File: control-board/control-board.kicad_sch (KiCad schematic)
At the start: 65 parts, among them J1 LED ch 1-16, J10 ESP32 left (3V3 row), J11 ESP32 right (GND row), J12 24V IN, J2 LED ch 17-32, J3 LED ch 33-48, J4 LED ch 49-64, J5 LED ch 65-80, J6 LED ch 81-96, J7 24V IN (5.5/2.5), J8 FAN 24V, J9 logic/analog, Q1 AO3400A, SW1 MODE, SW2 UP, SW3 DOWN, U101 PCA9685PW (0x40), U102 PCA9685PW (0x41), U103 PCA9685PW (0x42), U104 PCA9685PW (0x43), U105 PCA9685PW (0x44), U106 PCA9685PW (0x45), U110 XL1509-5.0E1, U111 ADS1115IDGS (DNP)

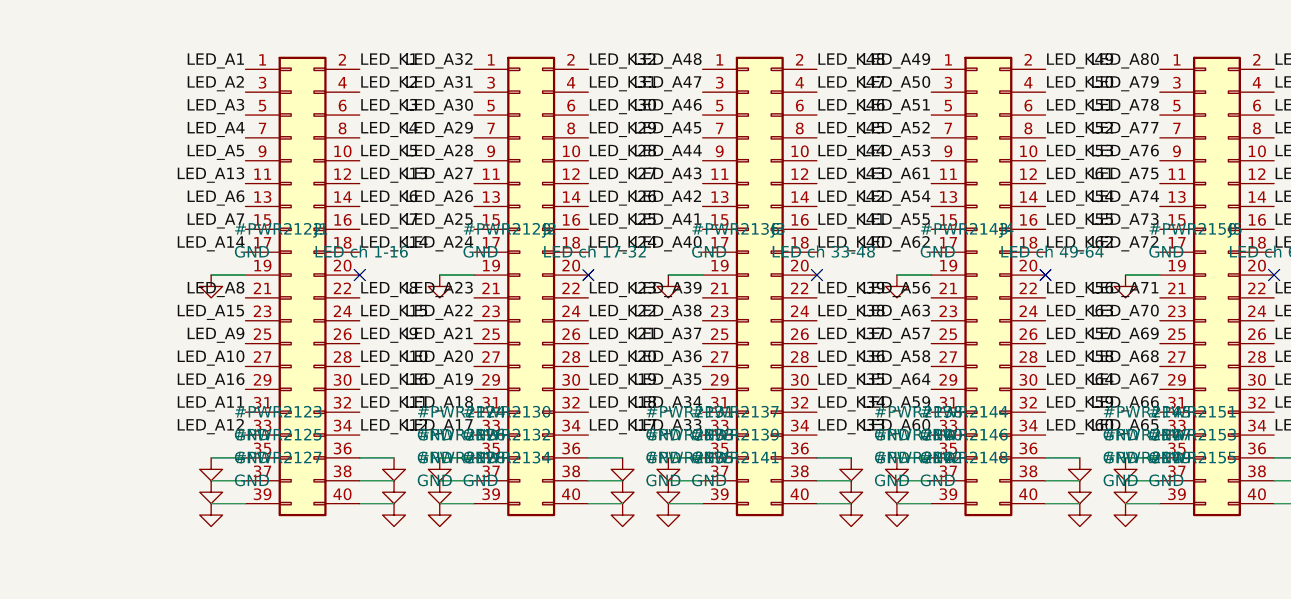
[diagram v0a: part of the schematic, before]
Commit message: LED board support parts copied to control-board topology (15mm border kept)
J1/J4 vertical on left edge, J2/J3 top, J5/J6 bottom, mux stack +
J9 on right strip; pin_maps v6 (CONN_MAP re-optimized, NTC_MAP
re-derived for right-strip muxes); schematics regenerated, netlists
verified, pads re-netted, zones refilled. New scripts:
layout_led_support.py, apply_netlist.py.

Co-Authored-By: Claude Fable 5 <noreply@anthropic.com>
Claude-Session: https://claude.ai/code/session_017oD54uh7Tvu54u9NPQNcZB
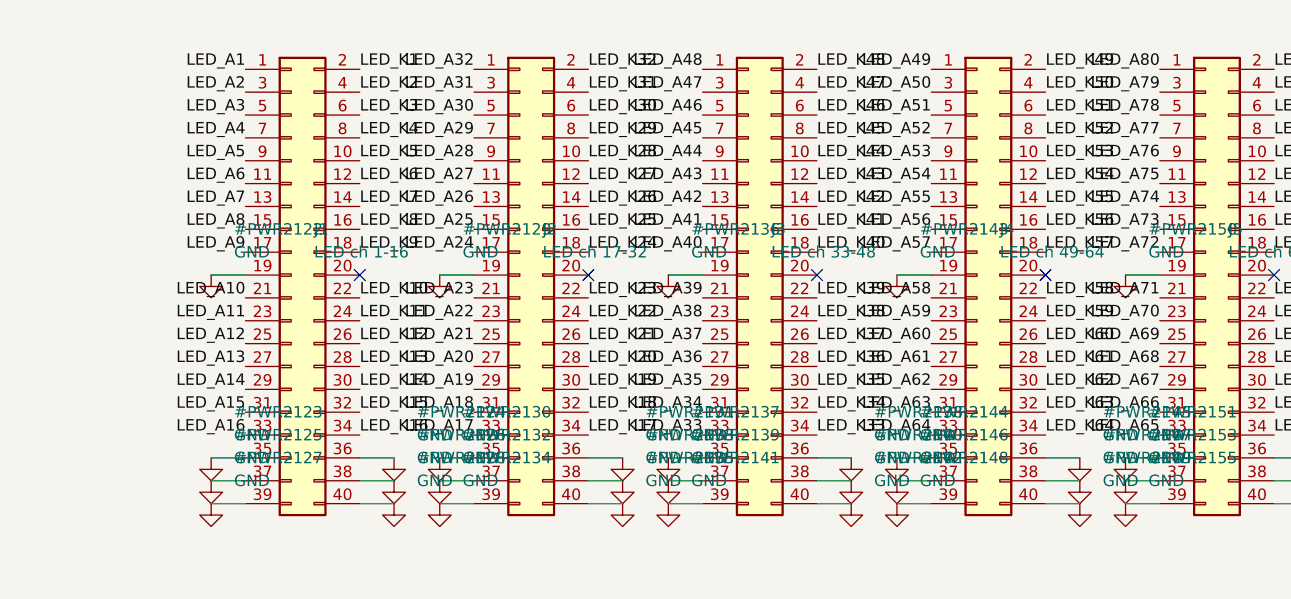
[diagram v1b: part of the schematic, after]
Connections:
- net LED_A10: now also J1.21 (Pin_21); no longer J1.27 (Pin_27)
- net LED_A11: now also J1.23 (Pin_23); no longer J1.31 (Pin_31)
- net LED_A12: now also J1.25 (Pin_25); no longer J1.33 (Pin_33)
- net LED_A13: now also J1.27 (Pin_27); no longer J1.11 (Pin_11)
- net LED_A14: now also J1.29 (Pin_29); no longer J1.17 (Pin_17)
- net LED_A15: now also J1.31 (Pin_31); no longer J1.23 (Pin_23)
- net LED_A16: now also J1.33 (Pin_33); no longer J1.29 (Pin_29)
- net LED_A54: now also J4.11 (Pin_11); no longer J4.13 (Pin_13)
- net LED_A55: now also J4.13 (Pin_13); no longer J4.15 (Pin_15)
- net LED_A56: now also J4.15 (Pin_15); no longer J4.21 (Pin_21)
- net LED_A57: now also J4.17 (Pin_17); no longer J4.25 (Pin_25)
- net LED_A58: now also J4.21 (Pin_21); no longer J4.27 (Pin_27)
- net LED_A59: now also J4.23 (Pin_23); no longer J4.31 (Pin_31)
- net LED_A6: now also J1.11 (Pin_11); no longer J1.13 (Pin_13)
- net LED_A60: now also J4.25 (Pin_25); no longer J4.33 (Pin_33)
- net LED_A61: now also J4.27 (Pin_27); no longer J4.11 (Pin_11)
- net LED_A62: now also J4.29 (Pin_29); no longer J4.17 (Pin_17)
- net LED_A63: now also J4.31 (Pin_31); no longer J4.23 (Pin_23)
- net LED_A64: now also J4.33 (Pin_33); no longer J4.29 (Pin_29)
- net LED_A7: now also J1.13 (Pin_13); no longer J1.15 (Pin_15)
- net LED_A8: now also J1.15 (Pin_15); no longer J1.21 (Pin_21)
- net LED_A9: now also J1.17 (Pin_17); no longer J1.25 (Pin_25)
- net LED_K10: now also J1.22 (Pin_22); no longer J1.28 (Pin_28)
- net LED_K11: now also J1.24 (Pin_24); no longer J1.32 (Pin_32)
- net LED_K12: now also J1.26 (Pin_26); no longer J1.34 (Pin_34)
- net LED_K13: now also J1.28 (Pin_28); no longer J1.12 (Pin_12)
- net LED_K14: now also J1.30 (Pin_30); no longer J1.18 (Pin_18)
- net LED_K15: now also J1.32 (Pin_32); no longer J1.24 (Pin_24)
- net LED_K16: now also J1.34 (Pin_34); no longer J1.30 (Pin_30)
- net LED_K54: now also J4.12 (Pin_12); no longer J4.14 (Pin_14)
- net LED_K55: now also J4.14 (Pin_14); no longer J4.16 (Pin_16)
- net LED_K56: now also J4.16 (Pin_16); no longer J4.22 (Pin_22)
- net LED_K57: now also J4.18 (Pin_18); no longer J4.26 (Pin_26)
- net LED_K58: now also J4.22 (Pin_22); no longer J4.28 (Pin_28)
- net LED_K59: now also J4.24 (Pin_24); no longer J4.32 (Pin_32)
- net LED_K6: now also J1.12 (Pin_12); no longer J1.14 (Pin_14)
- net LED_K60: now also J4.26 (Pin_26); no longer J4.34 (Pin_34)
- net LED_K61: now also J4.28 (Pin_28); no longer J4.12 (Pin_12)
- net LED_K62: now also J4.30 (Pin_30); no longer J4.18 (Pin_18)
- net LED_K63: now also J4.32 (Pin_32); no longer J4.24 (Pin_24)
- net LED_K64: now also J4.34 (Pin_34); no longer J4.30 (Pin_30)
- net LED_K7: now also J1.14 (Pin_14); no longer J1.16 (Pin_16)
- net LED_K8: now also J1.16 (Pin_16); no longer J1.22 (Pin_22)
- net LED_K9: now also J1.18 (Pin_18); no longer J1.26 (Pin_26)

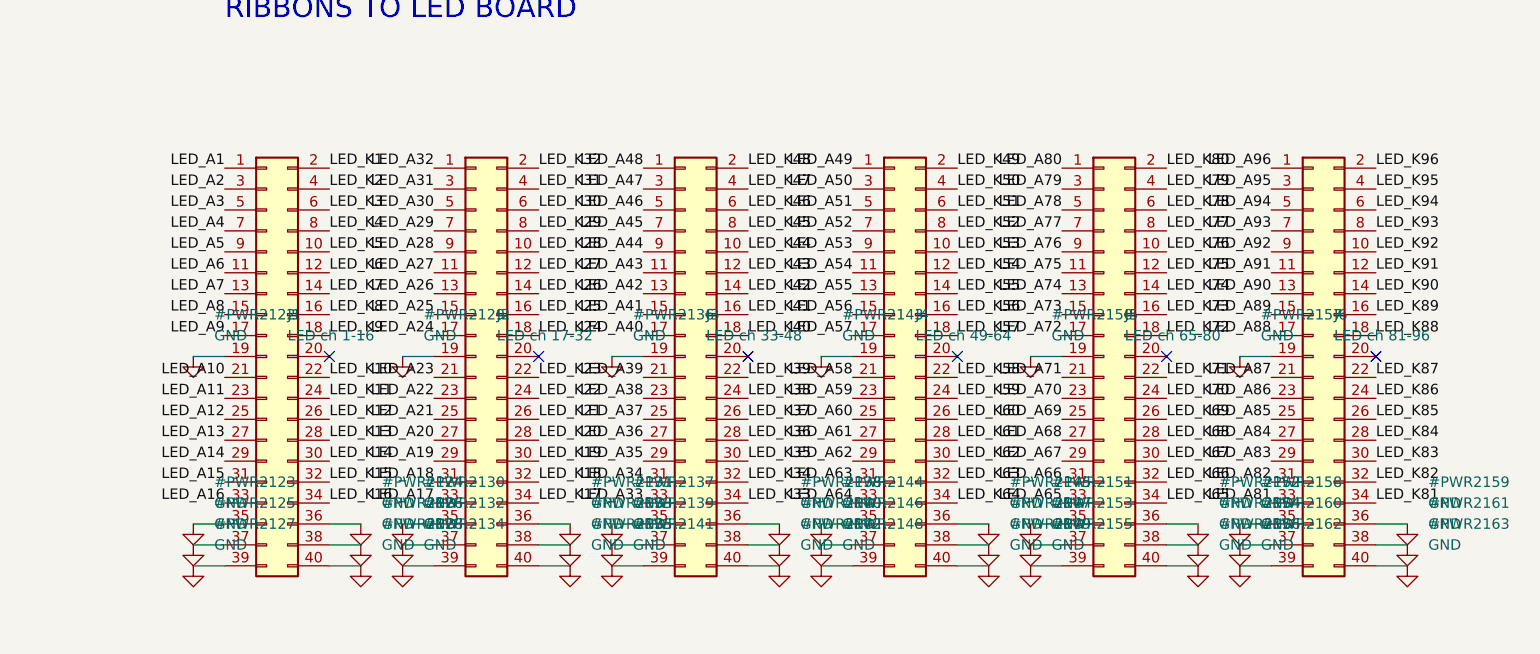
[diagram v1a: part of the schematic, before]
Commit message: LED-array pinout optimization: zero ribbon fan-out crossings + proximity NTC muxing
CONN_MAP -> LED-board-optimal nested pin order: fan-out crossings on the
LED board 536->0 across all six ribbons; control board near-Pareto
(440->464 inversions, J1/J4 improved to 0). Shared 1:1 cable respected.
NTC_MAP -> each mux takes its 16 nearest NTCs (proximity row-bands for the
right-edge stack): analog trace length -11% (8107->7222mm), horizontal
fan-in. PCA_MAP carried through unchanged (control-internal).

pin_maps v7; schematics regenerated; netlists ALL MATCH + cross-board OK;
286/192 pads re-netted; zones refilled. New: optimize_led_pins.py.

Co-Authored-By: Claude Fable 5 <noreply@anthropic.com>
Claude-Session: https://claude.ai/code/session_017oD54uh7Tvu54u9NPQNcZB
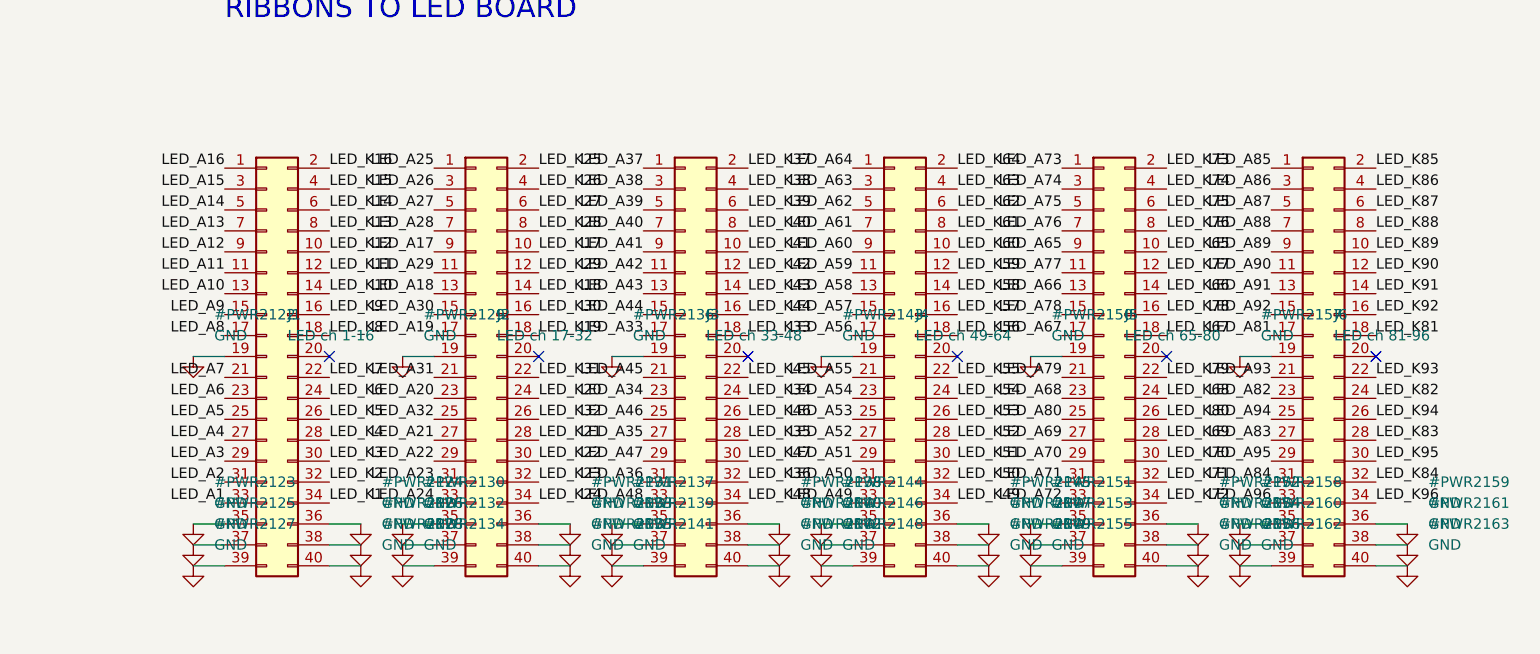
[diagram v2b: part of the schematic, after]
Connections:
- net LED_A1: now also J1.33 (Pin_33); no longer J1.1 (Pin_1)
- net LED_A10: now also J1.13 (Pin_13); no longer J1.21 (Pin_21)
- net LED_A11: now also J1.11 (Pin_11); no longer J1.23 (Pin_23)
- net LED_A12: now also J1.9 (Pin_9); no longer J1.25 (Pin_25)
- net LED_A13: now also J1.7 (Pin_7); no longer J1.27 (Pin_27)
- net LED_A14: now also J1.5 (Pin_5); no longer J1.29 (Pin_29)
- net LED_A15: now also J1.3 (Pin_3); no longer J1.31 (Pin_31)
- net LED_A16: now also J1.1 (Pin_1); no longer J1.33 (Pin_33)
- net LED_A17: now also J2.9 (Pin_9); no longer J2.33 (Pin_33)
- net LED_A18: now also J2.13 (Pin_13); no longer J2.31 (Pin_31)
- net LED_A19: now also J2.17 (Pin_17); no longer J2.29 (Pin_29)
- net LED_A2: now also J1.31 (Pin_31); no longer J1.3 (Pin_3)
- net LED_A20: now also J2.23 (Pin_23); no longer J2.27 (Pin_27)
- net LED_A21: now also J2.27 (Pin_27); no longer J2.25 (Pin_25)
- net LED_A22: now also J2.29 (Pin_29); no longer J2.23 (Pin_23)
- net LED_A23: now also J2.31 (Pin_31); no longer J2.21 (Pin_21)
- net LED_A24: now also J2.33 (Pin_33); no longer J2.17 (Pin_17)
- net LED_A25: now also J2.1 (Pin_1); no longer J2.15 (Pin_15)
- net LED_A26: now also J2.3 (Pin_3); no longer J2.13 (Pin_13)
- net LED_A27: now also J2.5 (Pin_5); no longer J2.11 (Pin_11)
- net LED_A28: now also J2.7 (Pin_7); no longer J2.9 (Pin_9)
- net LED_A29: now also J2.11 (Pin_11); no longer J2.7 (Pin_7)
- net LED_A3: now also J1.29 (Pin_29); no longer J1.5 (Pin_5)
- net LED_A30: now also J2.15 (Pin_15); no longer J2.5 (Pin_5)
- net LED_A31: now also J2.21 (Pin_21); no longer J2.3 (Pin_3)
- net LED_A32: now also J2.25 (Pin_25); no longer J2.1 (Pin_1)
- net LED_A33: now also J3.17 (Pin_17); no longer J3.33 (Pin_33)
- net LED_A34: now also J3.23 (Pin_23); no longer J3.31 (Pin_31)
- net LED_A35: now also J3.27 (Pin_27); no longer J3.29 (Pin_29)
- net LED_A36: now also J3.31 (Pin_31); no longer J3.27 (Pin_27)
- net LED_A37: now also J3.1 (Pin_1); no longer J3.25 (Pin_25)
- net LED_A38: now also J3.3 (Pin_3); no longer J3.23 (Pin_23)
- net LED_A39: now also J3.5 (Pin_5); no longer J3.21 (Pin_21)
- net LED_A4: now also J1.27 (Pin_27); no longer J1.7 (Pin_7)
- net LED_A40: now also J3.7 (Pin_7); no longer J3.17 (Pin_17)
- net LED_A41: now also J3.9 (Pin_9); no longer J3.15 (Pin_15)
- net LED_A42: now also J3.11 (Pin_11); no longer J3.13 (Pin_13)
- net LED_A43: now also J3.13 (Pin_13); no longer J3.11 (Pin_11)
- net LED_A44: now also J3.15 (Pin_15); no longer J3.9 (Pin_9)
- net LED_A45: now also J3.21 (Pin_21); no longer J3.7 (Pin_7)
- net LED_A46: now also J3.25 (Pin_25); no longer J3.5 (Pin_5)
- net LED_A47: now also J3.29 (Pin_29); no longer J3.3 (Pin_3)
- net LED_A48: now also J3.33 (Pin_33); no longer J3.1 (Pin_1)
- net LED_A49: now also J4.33 (Pin_33); no longer J4.1 (Pin_1)
- net LED_A5: now also J1.25 (Pin_25); no longer J1.9 (Pin_9)
- net LED_A50: now also J4.31 (Pin_31); no longer J4.3 (Pin_3)
- net LED_A51: now also J4.29 (Pin_29); no longer J4.5 (Pin_5)
- net LED_A52: now also J4.27 (Pin_27); no longer J4.7 (Pin_7)
- net LED_A53: now also J4.25 (Pin_25); no longer J4.9 (Pin_9)
- net LED_A54: now also J4.23 (Pin_23); no longer J4.11 (Pin_11)
- net LED_A55: now also J4.21 (Pin_21); no longer J4.13 (Pin_13)
- net LED_A56: now also J4.17 (Pin_17); no longer J4.15 (Pin_15)
- net LED_A57: now also J4.15 (Pin_15); no longer J4.17 (Pin_17)
- net LED_A58: now also J4.13 (Pin_13); no longer J4.21 (Pin_21)
- net LED_A59: now also J4.11 (Pin_11); no longer J4.23 (Pin_23)
- net LED_A6: now also J1.23 (Pin_23); no longer J1.11 (Pin_11)
- net LED_A60: now also J4.9 (Pin_9); no longer J4.25 (Pin_25)
- net LED_A61: now also J4.7 (Pin_7); no longer J4.27 (Pin_27)
- net LED_A62: now also J4.5 (Pin_5); no longer J4.29 (Pin_29)
- net LED_A63: now also J4.3 (Pin_3); no longer J4.31 (Pin_31)
- net LED_A64: now also J4.1 (Pin_1); no longer J4.33 (Pin_33)
- net LED_A65: now also J5.9 (Pin_9); no longer J5.33 (Pin_33)
- net LED_A66: now also J5.13 (Pin_13); no longer J5.31 (Pin_31)
- net LED_A67: now also J5.17 (Pin_17); no longer J5.29 (Pin_29)
- net LED_A68: now also J5.23 (Pin_23); no longer J5.27 (Pin_27)
- net LED_A69: now also J5.27 (Pin_27); no longer J5.25 (Pin_25)
- net LED_A7: now also J1.21 (Pin_21); no longer J1.13 (Pin_13)
- net LED_A70: now also J5.29 (Pin_29); no longer J5.23 (Pin_23)
- net LED_A71: now also J5.31 (Pin_31); no longer J5.21 (Pin_21)
- net LED_A72: now also J5.33 (Pin_33); no longer J5.17 (Pin_17)
- net LED_A73: now also J5.1 (Pin_1); no longer J5.15 (Pin_15)
- net LED_A74: now also J5.3 (Pin_3); no longer J5.13 (Pin_13)
- net LED_A75: now also J5.5 (Pin_5); no longer J5.11 (Pin_11)
- net LED_A76: now also J5.7 (Pin_7); no longer J5.9 (Pin_9)
- net LED_A77: now also J5.11 (Pin_11); no longer J5.7 (Pin_7)
- net LED_A78: now also J5.15 (Pin_15); no longer J5.5 (Pin_5)
- net LED_A79: now also J5.21 (Pin_21); no longer J5.3 (Pin_3)
- net LED_A8: now also J1.17 (Pin_17); no longer J1.15 (Pin_15)
- net LED_A80: now also J5.25 (Pin_25); no longer J5.1 (Pin_1)
- net LED_A81: now also J6.17 (Pin_17); no longer J6.33 (Pin_33)
- net LED_A82: now also J6.23 (Pin_23); no longer J6.31 (Pin_31)
- net LED_A83: now also J6.27 (Pin_27); no longer J6.29 (Pin_29)
- net LED_A84: now also J6.31 (Pin_31); no longer J6.27 (Pin_27)
- net LED_A85: now also J6.1 (Pin_1); no longer J6.25 (Pin_25)
- net LED_A86: now also J6.3 (Pin_3); no longer J6.23 (Pin_23)
- net LED_A87: now also J6.5 (Pin_5); no longer J6.21 (Pin_21)
- net LED_A88: now also J6.7 (Pin_7); no longer J6.17 (Pin_17)
- net LED_A89: now also J6.9 (Pin_9); no longer J6.15 (Pin_15)
- net LED_A9: now also J1.15 (Pin_15); no longer J1.17 (Pin_17)
- net LED_A90: now also J6.11 (Pin_11); no longer J6.13 (Pin_13)
- net LED_A91: now also J6.13 (Pin_13); no longer J6.11 (Pin_11)
- net LED_A92: now also J6.15 (Pin_15); no longer J6.9 (Pin_9)
- net LED_A93: now also J6.21 (Pin_21); no longer J6.7 (Pin_7)
- net LED_A94: now also J6.25 (Pin_25); no longer J6.5 (Pin_5)
- net LED_A95: now also J6.29 (Pin_29); no longer J6.3 (Pin_3)
- net LED_A96: now also J6.33 (Pin_33); no longer J6.1 (Pin_1)
- net LED_K1: now also J1.34 (Pin_34); no longer J1.2 (Pin_2)
- net LED_K10: now also J1.14 (Pin_14); no longer J1.22 (Pin_22)
- net LED_K11: now also J1.12 (Pin_12); no longer J1.24 (Pin_24)
- net LED_K12: now also J1.10 (Pin_10); no longer J1.26 (Pin_26)
- net LED_K13: now also J1.8 (Pin_8); no longer J1.28 (Pin_28)
- net LED_K14: now also J1.6 (Pin_6); no longer J1.30 (Pin_30)
- net LED_K15: now also J1.4 (Pin_4); no longer J1.32 (Pin_32)
- net LED_K16: now also J1.2 (Pin_2); no longer J1.34 (Pin_34)
- net LED_K17: now also J2.10 (Pin_10); no longer J2.34 (Pin_34)
- net LED_K18: now also J2.14 (Pin_14); no longer J2.32 (Pin_32)
- net LED_K19: now also J2.18 (Pin_18); no longer J2.30 (Pin_30)
- net LED_K2: now also J1.32 (Pin_32); no longer J1.4 (Pin_4)
- net LED_K20: now also J2.24 (Pin_24); no longer J2.28 (Pin_28)
- net LED_K21: now also J2.28 (Pin_28); no longer J2.26 (Pin_26)
- net LED_K22: now also J2.30 (Pin_30); no longer J2.24 (Pin_24)
- net LED_K23: now also J2.32 (Pin_32); no longer J2.22 (Pin_22)
- net LED_K24: now also J2.34 (Pin_34); no longer J2.18 (Pin_18)
- net LED_K25: now also J2.2 (Pin_2); no longer J2.16 (Pin_16)
- net LED_K26: now also J2.4 (Pin_4); no longer J2.14 (Pin_14)
- net LED_K27: now also J2.6 (Pin_6); no longer J2.12 (Pin_12)
- net LED_K28: now also J2.8 (Pin_8); no longer J2.10 (Pin_10)
- net LED_K29: now also J2.12 (Pin_12); no longer J2.8 (Pin_8)
- net LED_K3: now also J1.30 (Pin_30); no longer J1.6 (Pin_6)
- net LED_K30: now also J2.16 (Pin_16); no longer J2.6 (Pin_6)
- net LED_K31: now also J2.22 (Pin_22); no longer J2.4 (Pin_4)
- net LED_K32: now also J2.26 (Pin_26); no longer J2.2 (Pin_2)
- net LED_K33: now also J3.18 (Pin_18); no longer J3.34 (Pin_34)
- net LED_K34: now also J3.24 (Pin_24); no longer J3.32 (Pin_32)
- net LED_K35: now also J3.28 (Pin_28); no longer J3.30 (Pin_30)
- net LED_K36: now also J3.32 (Pin_32); no longer J3.28 (Pin_28)
- net LED_K37: now also J3.2 (Pin_2); no longer J3.26 (Pin_26)
- net LED_K38: now also J3.4 (Pin_4); no longer J3.24 (Pin_24)
- net LED_K39: now also J3.6 (Pin_6); no longer J3.22 (Pin_22)
- net LED_K4: now also J1.28 (Pin_28); no longer J1.8 (Pin_8)
- net LED_K40: now also J3.8 (Pin_8); no longer J3.18 (Pin_18)
- net LED_K41: now also J3.10 (Pin_10); no longer J3.16 (Pin_16)
- net LED_K42: now also J3.12 (Pin_12); no longer J3.14 (Pin_14)
- net LED_K43: now also J3.14 (Pin_14); no longer J3.12 (Pin_12)
- net LED_K44: now also J3.16 (Pin_16); no longer J3.10 (Pin_10)
- net LED_K45: now also J3.22 (Pin_22); no longer J3.8 (Pin_8)
- net LED_K46: now also J3.26 (Pin_26); no longer J3.6 (Pin_6)
- net LED_K47: now also J3.30 (Pin_30); no longer J3.4 (Pin_4)
- net LED_K48: now also J3.34 (Pin_34); no longer J3.2 (Pin_2)
- net LED_K49: now also J4.34 (Pin_34); no longer J4.2 (Pin_2)
- net LED_K5: now also J1.26 (Pin_26); no longer J1.10 (Pin_10)
- net LED_K50: now also J4.32 (Pin_32); no longer J4.4 (Pin_4)
- net LED_K51: now also J4.30 (Pin_30); no longer J4.6 (Pin_6)
- net LED_K52: now also J4.28 (Pin_28); no longer J4.8 (Pin_8)
- net LED_K53: now also J4.26 (Pin_26); no longer J4.10 (Pin_10)
- net LED_K54: now also J4.24 (Pin_24); no longer J4.12 (Pin_12)
- net LED_K55: now also J4.22 (Pin_22); no longer J4.14 (Pin_14)
- net LED_K56: now also J4.18 (Pin_18); no longer J4.16 (Pin_16)
- net LED_K57: now also J4.16 (Pin_16); no longer J4.18 (Pin_18)
- net LED_K58: now also J4.14 (Pin_14); no longer J4.22 (Pin_22)
- net LED_K59: now also J4.12 (Pin_12); no longer J4.24 (Pin_24)
- net LED_K6: now also J1.24 (Pin_24); no longer J1.12 (Pin_12)
- net LED_K60: now also J4.10 (Pin_10); no longer J4.26 (Pin_26)
- net LED_K61: now also J4.8 (Pin_8); no longer J4.28 (Pin_28)
- net LED_K62: now also J4.6 (Pin_6); no longer J4.30 (Pin_30)
- net LED_K63: now also J4.4 (Pin_4); no longer J4.32 (Pin_32)
- net LED_K64: now also J4.2 (Pin_2); no longer J4.34 (Pin_34)
- net LED_K65: now also J5.10 (Pin_10); no longer J5.34 (Pin_34)
- net LED_K66: now also J5.14 (Pin_14); no longer J5.32 (Pin_32)
- net LED_K67: now also J5.18 (Pin_18); no longer J5.30 (Pin_30)
- net LED_K68: now also J5.24 (Pin_24); no longer J5.28 (Pin_28)
- net LED_K69: now also J5.28 (Pin_28); no longer J5.26 (Pin_26)
- net LED_K7: now also J1.22 (Pin_22); no longer J1.14 (Pin_14)
- net LED_K70: now also J5.30 (Pin_30); no longer J5.24 (Pin_24)
- net LED_K71: now also J5.32 (Pin_32); no longer J5.22 (Pin_22)
- net LED_K72: now also J5.34 (Pin_34); no longer J5.18 (Pin_18)
- net LED_K73: now also J5.2 (Pin_2); no longer J5.16 (Pin_16)
- net LED_K74: now also J5.4 (Pin_4); no longer J5.14 (Pin_14)
- net LED_K75: now also J5.6 (Pin_6); no longer J5.12 (Pin_12)
- net LED_K76: now also J5.8 (Pin_8); no longer J5.10 (Pin_10)
- net LED_K77: now also J5.12 (Pin_12); no longer J5.8 (Pin_8)
- net LED_K78: now also J5.16 (Pin_16); no longer J5.6 (Pin_6)
- net LED_K79: now also J5.22 (Pin_22); no longer J5.4 (Pin_4)
- net LED_K8: now also J1.18 (Pin_18); no longer J1.16 (Pin_16)
- net LED_K80: now also J5.26 (Pin_26); no longer J5.2 (Pin_2)
- net LED_K81: now also J6.18 (Pin_18); no longer J6.34 (Pin_34)
- net LED_K82: now also J6.24 (Pin_24); no longer J6.32 (Pin_32)
- net LED_K83: now also J6.28 (Pin_28); no longer J6.30 (Pin_30)
- net LED_K84: now also J6.32 (Pin_32); no longer J6.28 (Pin_28)
- net LED_K85: now also J6.2 (Pin_2); no longer J6.26 (Pin_26)
- net LED_K86: now also J6.4 (Pin_4); no longer J6.24 (Pin_24)
- net LED_K87: now also J6.6 (Pin_6); no longer J6.22 (Pin_22)
- net LED_K88: now also J6.8 (Pin_8); no longer J6.18 (Pin_18)
- net LED_K89: now also J6.10 (Pin_10); no longer J6.16 (Pin_16)
- net LED_K9: now also J1.16 (Pin_16); no longer J1.18 (Pin_18)
- net LED_K90: now also J6.12 (Pin_12); no longer J6.14 (Pin_14)
- net LED_K91: now also J6.14 (Pin_14); no longer J6.12 (Pin_12)
- net LED_K92: now also J6.16 (Pin_16); no longer J6.10 (Pin_10)
- net LED_K93: now also J6.22 (Pin_22); no longer J6.8 (Pin_8)
- net LED_K94: now also J6.26 (Pin_26); no longer J6.6 (Pin_6)
- net LED_K95: now also J6.30 (Pin_30); no longer J6.4 (Pin_4)
- net LED_K96: now also J6.34 (Pin_34); no longer J6.2 (Pin_2)
